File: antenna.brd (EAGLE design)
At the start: 98 x 98 mm, 21 parts, among them X1 BU-SMA-V

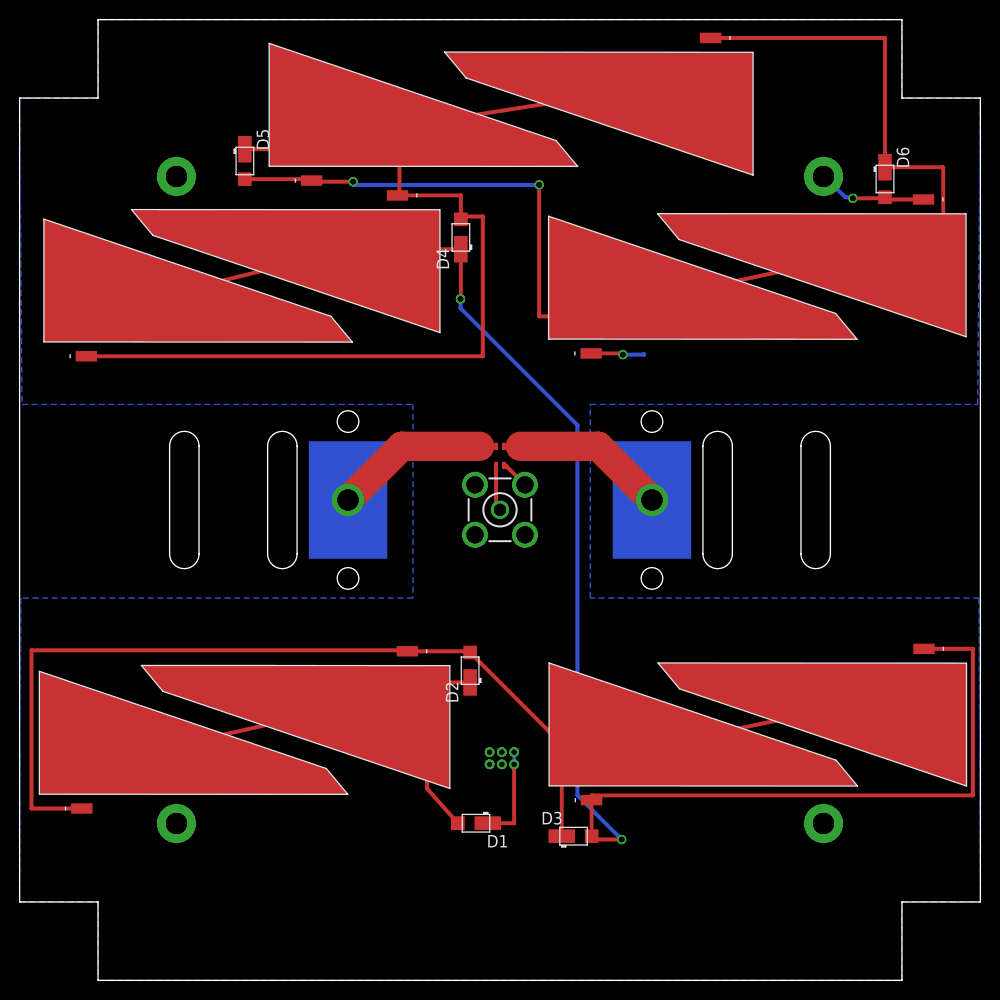
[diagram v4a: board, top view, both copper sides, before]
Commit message: Antenna board tweaks
Changed connectors, fixed solar panel mirroring issue
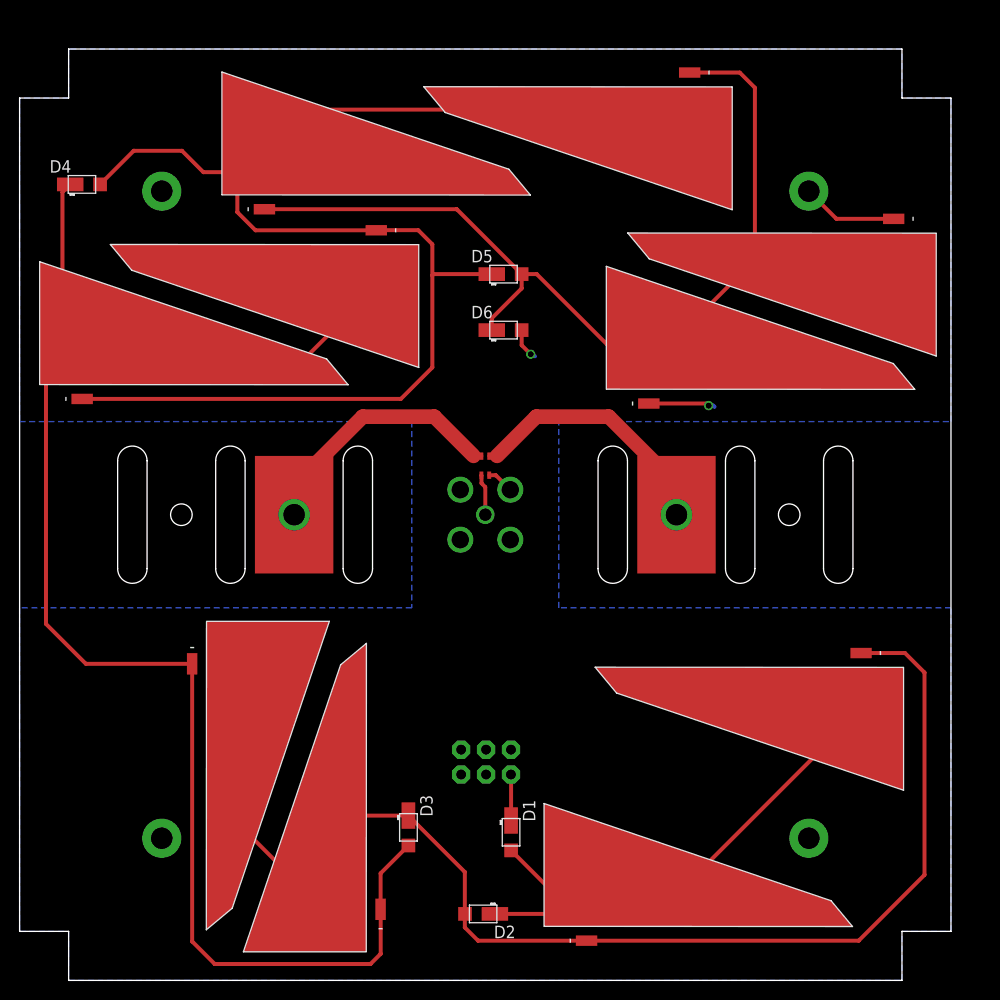
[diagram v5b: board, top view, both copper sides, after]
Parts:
- removed U$4: G125-FV20605L0P, G125-FV20605L0P:G125-FV20605L0P
- added JP1: (no value), SparkFun-Connectors:2X3
- moved SL2 74.6 mm to (82.8, 31.8), turned to 270 degrees
- moved SL4 70.1 mm to (19.2, 29.3), turned to 0 degrees
- moved D6 41.9 mm to (49.4, 66.3), turned to 0 degrees
- moved D4 39.0 mm to (6.36, 81.2), turned to 0 degrees
- moved SL1 35.8 mm to (60.8, 5.64), turned to 90 degrees
- moved D5 28.8 mm to (49.4, 72.0), turned to 0 degrees
- moved SL3 27.9 mm to (35.2, 10.2), turned to 180 degrees
- moved D2 24.8 mm to (47.3, 6.78), turned to 180 degrees
- moved D3 16.9 mm to (39.7, 15.6), turned to 270 degrees
- moved SL10 7.80 mm to (67.2, 60.4)
- moved U$1 5.70 mm to (28.0, 47.5), flipped to the top
- moved SL8 5.64 mm to (28.0, 80.2)
- moved SL6 4.37 mm to (9.38, 60.9)
- moved SL5 4.16 mm to (33.4, 74.9)
- moved SL7 4.12 mm to (65.3, 91.0)
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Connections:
- net N$2 renamed RFN
- net N$3 renamed RFP
- net GND: no longer U$4.P1, U$4.P4
- net V_SOLAR: now also JP1.1; no longer U$4.P3, U$4.P6
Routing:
- net N$39: track 124.0 -> 148.2 mm
- net N$50: track 130.1 -> 109.7 mm, vias 2 -> 0
- net N$37: track 175.2 -> 161.6 mm, vias 2 -> 0
- net N$45: track 129.9 -> 140.8 mm
- net RFP: track 17.4 -> 26.7 mm
- net RFN: track 17.4 -> 26.7 mm
- net V_SOLAR: track 9.94 -> 4.69 mm
- net GND: track 20.4 -> 22.8 mm
- net N$9: track 58.1 -> 56.8 mm
- net N$1: track 4.69 -> 4.19 mm
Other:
- board size 98 x 98 mm -> 95 x 95 mm
- board text removed: "Antenna Board V1.1"

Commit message: Antenna board connector fix
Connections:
- net GND: now also JP1.2
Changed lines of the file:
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@@
 <wire x1="52.13" y1="63.87" x2="52.35" y2="63.87" width="0.4064" layer="16"/>
 <wire x1="52.35" y1="63.87" x2="52.56" y2="63.66" width="0.4064" layer="16"/>
+<contactref element="JP1" pad="2"/>
 </signal>
 <signal name="RFN">
